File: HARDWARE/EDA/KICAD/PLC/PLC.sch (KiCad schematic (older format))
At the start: 62 parts

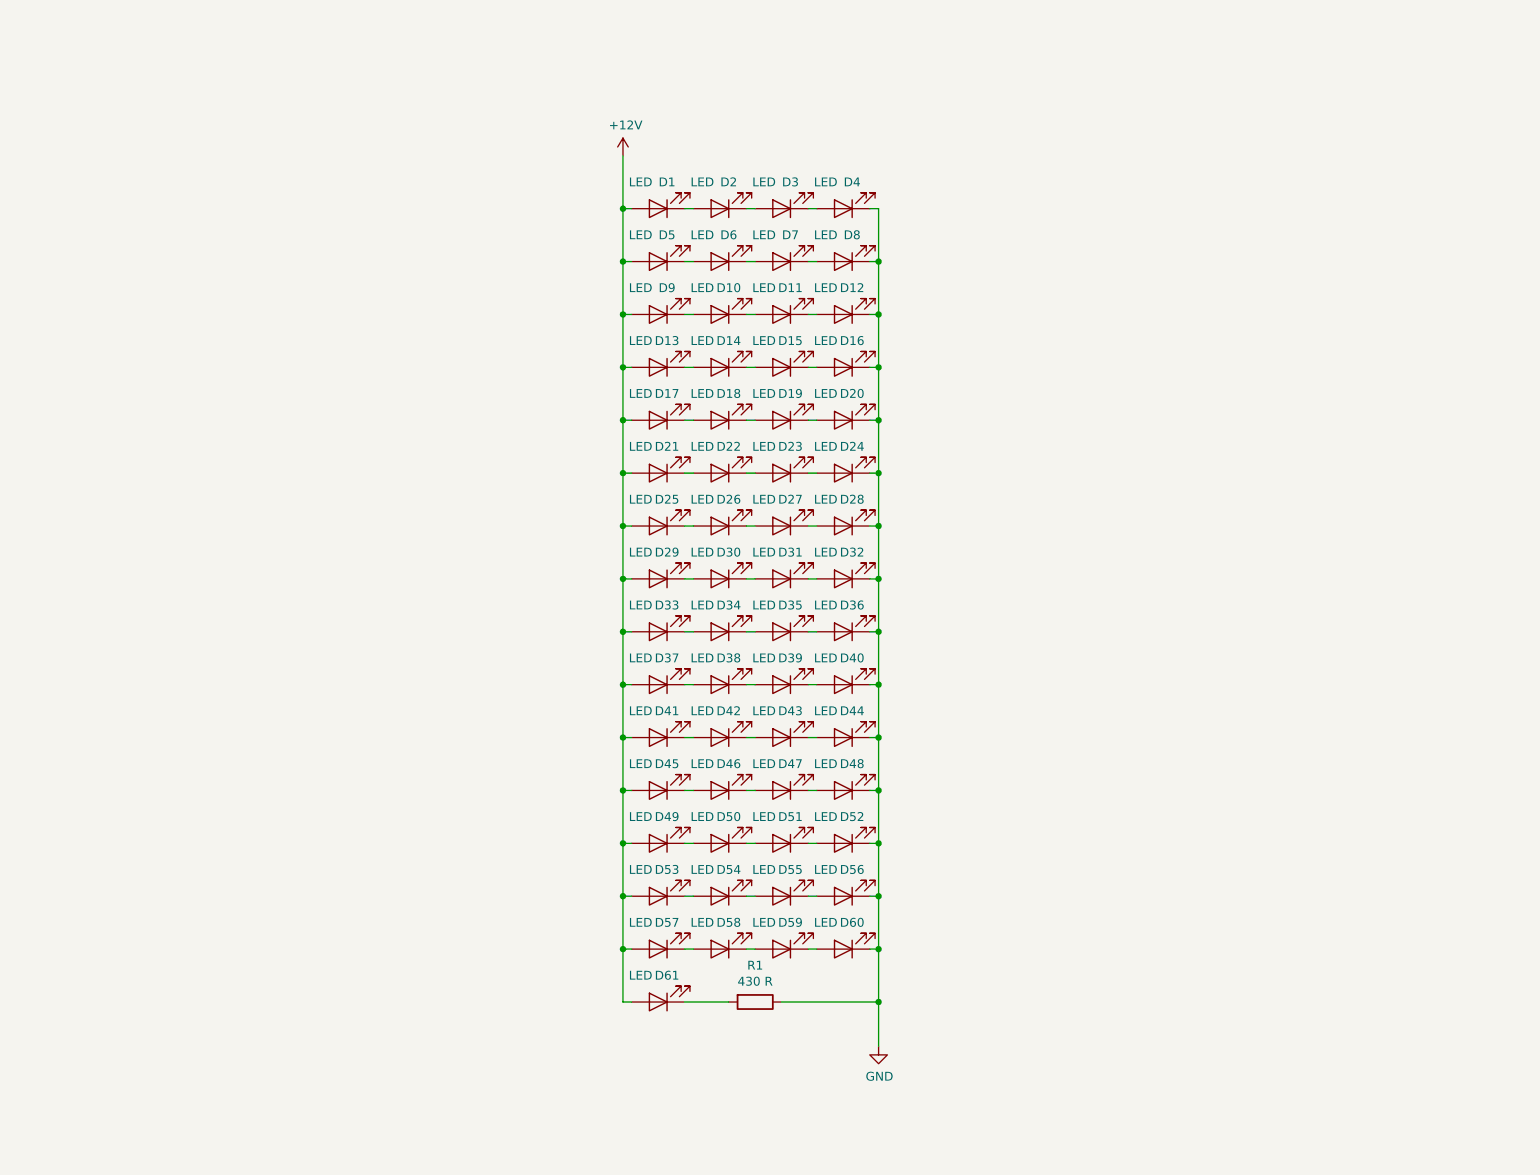
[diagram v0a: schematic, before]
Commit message: add files to toggle switch, add new componnents to plc
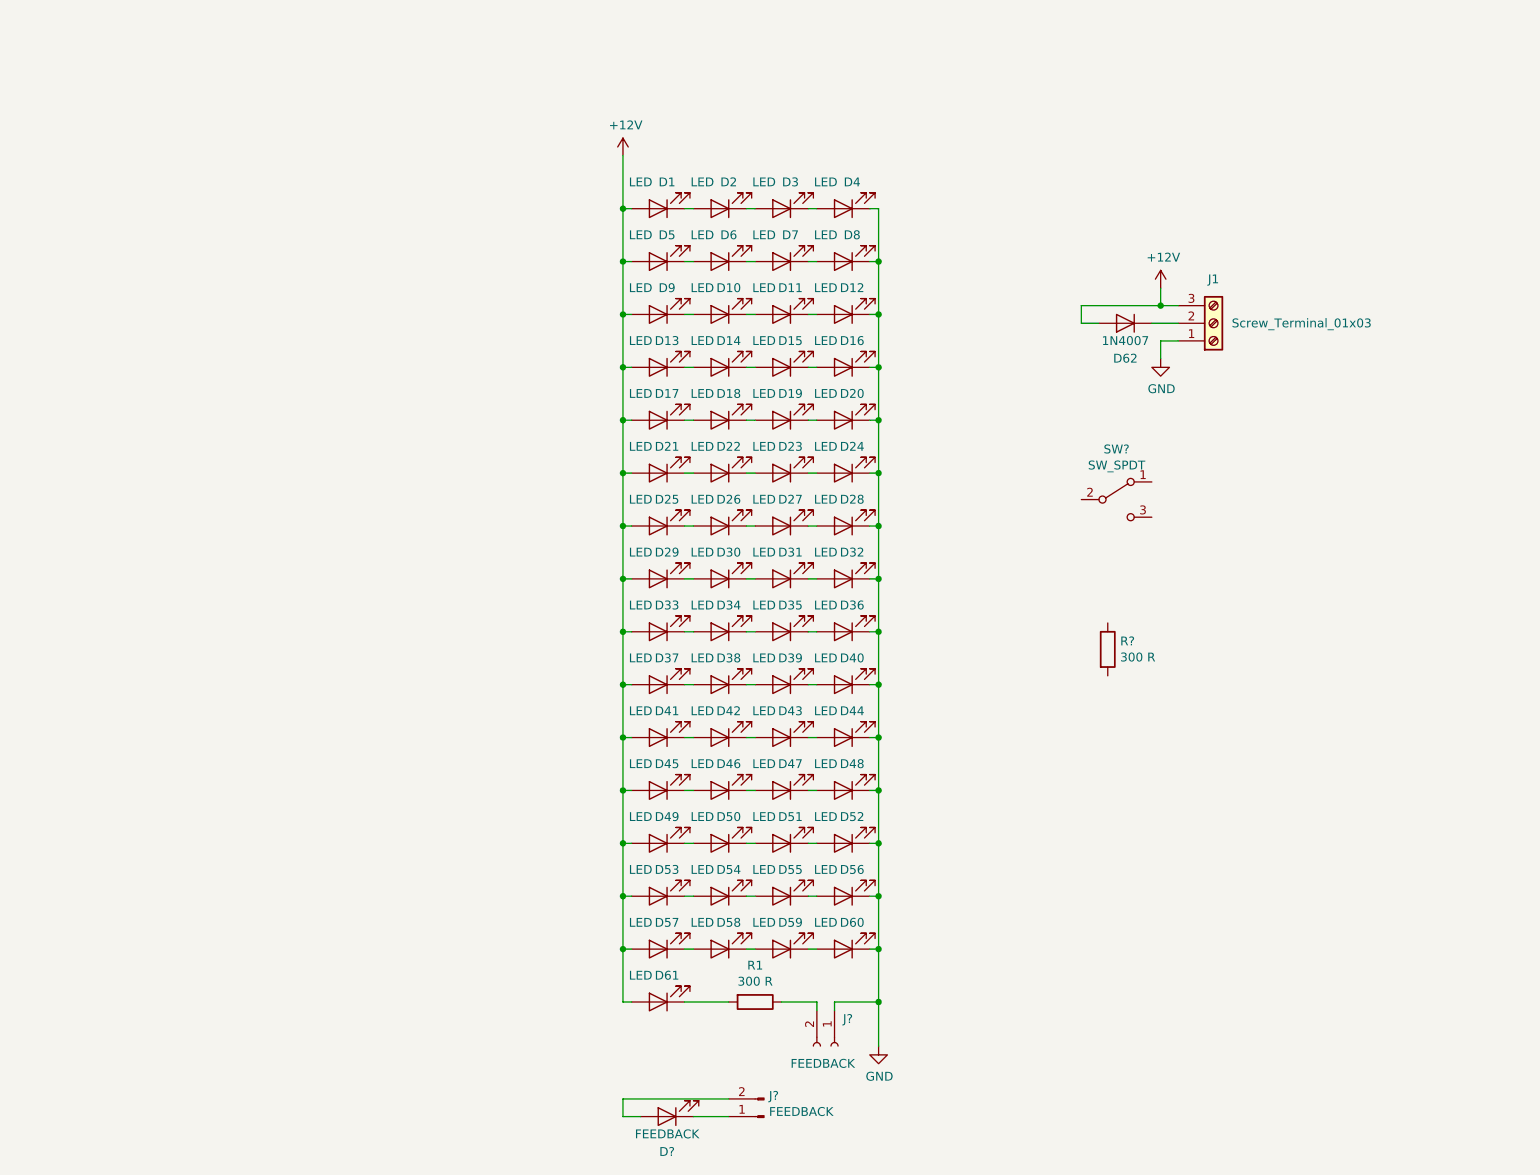
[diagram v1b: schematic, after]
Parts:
- added D62: 1N4007, Diode_THT:D_DO-41_SOD81_P10.16mm_Horizontal, symbol Diode:1N4007
- added D?: FEEDBACK, LED_THT:LED_D5.0mm_IRGrey, symbol Device:LED
- added J1: Screw_Terminal_01x03, Connector_Phoenix_MSTB:PhoenixContact_MSTBVA_2,5_3-G-5,08_1x03_P5.08mm_Vertical, symbol Connector:Screw_Terminal_01x03
- added J?: FEEDBACK, Connector_PinSocket_2.54mm:PinSocket_1x02_P2.54mm_Vertical, symbol Connector:Conn_01x02_Female
- added J?: FEEDBACK, symbol Connector:Conn_01x02_Male
- added R?: 300 R, Resistor_THT:R_Axial_DIN0411_L9.9mm_D3.6mm_P15.24mm_Horizontal, symbol Device:R
- added SW?: SW_SPDT, symbol Switch:SW_SPDT
- R1: value 430 R -> 300 R
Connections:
- net +12V: now also D62.2 (A), J1.3 (Pin_3)
- net GND: now also J1.1 (Pin_1), J?.1 (Pin_1); no longer R1.1
- new net: D62.1 (K), J1.2 (Pin_2)
- new net: J?.2 (Pin_2), R1.1
- new net: D?.1 (K), J?.1 (Pin_1)
- new net: D?.2 (A), J?.2 (Pin_2)
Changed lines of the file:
@@
 P 5200 6800
 F 0 "R1" V 4993 6800 50  0000 C CNN
-F 1 "430 R" V 5084 6800 50  0000 C CNN
+F 1 "300 R" V 5084 6800 50  0000 C CNN
 F 2 "Resistor_THT:R_Axial_DIN0207_L6.3mm_D2.5mm_P7.62mm_Horizontal" V 5130 6800 50  0001 C CNN
 F 3 "~" H 5200 6800 50  0001 C CNN
@@
 	4800 6800 5050 6800
 Wire Wire Line
-	5350 6800 5900 6800
+	5350 6800 5550 6800
 Wire Wire Line
 	4450 6800 4450 6500
@@
 	1    0    0    -1
 $EndComp
+$Comp
+L Connector:Screw_Terminal_01x03 J1
+U 1 1 61ADDB70
+P 7800 2950
+F 0 "J1" H 7800 2700 50  0000 C CNN
+F 1 "Screw_Terminal_01x03" H 8300 2950 50  0000 C CNN
+F 2 "Connector_Phoenix_MSTB:PhoenixContact_MSTBVA_2,5_3-G-5,08_1x03_P5.08mm_Vertical" H 7800 2950 50  0001 C CNN
+F 3 "~" H 7800 2950 50  0001 C CNN
+	1    7800 2950
+	1    0    0    1
+$EndComp
+$Comp
+L power:+12V #PWR03
+U 1 1 61AE4D2C
+P 7500 2750
+F 0 "#PWR03" H 7500 2600 50  0001 C CNN
+F 1 "+12V" H 7515 2923 50  0000 C CNN
+F 2 "" H 7500 2750 50  0001 C CNN
+F 3 "" H 7500 2750 50  0001 C CNN
+	1    7500 2750
+	1    0    0    -1
+$EndComp
+Wire Wire Line
+	7500 2750 7500 2850
+Wire Wire Line
+	7500 2850 7600 2850
+Wire Wire Line
+	7500 3050 7600 3050
+Connection ~ 7500 2850
+Wire Wire Line
+	7500 3150 7500 3050
+Wire Wire Line
+	7500 2850 7050 2850
+$Comp
+L power:GND #PWR04
+U 1 1 61AEFD3B
+P 7500 3150
+F 0 "#PWR04" H 7500 2900 50  0001 C CNN
+F 1 "GND" H 7505 2977 50  0000 C CNN
+F 2 "" H 7500 3150 50  0001 C CNN
+F 3 "" H 7500 3150 50  0001 C CNN
+	1    7500 3150
+	1    0    0    -1
+$EndComp
+$Comp
+L Device:LED D?
+U 1 1 61B68F6E
+P 4700 7450
+F 0 "D?" H 4700 7650 50  0000 C CNN
+F 1 "FEEDBACK" H 4700 7550 50  0000 C CNN
+F 2 "LED_THT:LED_D5.0mm_IRGrey" H 4700 7450 50  0001 C CNN
+F 3 "~" H 4700 7450 50  0001 C CNN
+	1    4700 7450
+	-1   0    0    1
+$EndComp
+$Comp
+L Diode:1N4007 D62
+U 1 1 61B4B3DB
+P 7300 2950
+F 0 "D62" H 7300 3150 50  0000 C CNN
+F 1 "1N4007" H 7300 3050 50  0000 C CNN
+F 2 "Diode_THT:D_DO-41_SOD81_P10.16mm_Horizontal" H 7300 2775 50  0001 C CNN
+F 3 "http://www.vishay.com/docs/88503/1n4001.pdf" H 7300 2950 50  0001 C CNN
+	1    7300 2950
+	-1   0    0    1
+$EndComp
+Wire Wire Line
+	7050 2950 7150 2950
+Wire Wire Line
+	7050 2850 7050 2950
+Wire Wire Line
+	7450 2950 7600 2950
+$Comp
+L Connector:Conn_01x02_Female J?
+U 1 1 61C04E26
+P 5650 7050
+F 0 "J?" V 5496 7098 50  0000 L CNN
+F 1 "FEEDBACK" V 5750 6800 50  0000 L CNN
+F 2 "Connector_PinSocket_2.54mm:PinSocket_1x02_P2.54mm_Vertical" H 5650 7050 50  0001 C CNN
+F 3 "~" H 5650 7050 50  0001 C CNN
+	1    5650 7050
+	0    1    1    0
+$EndComp
+Wire Wire Line
+	5550 6850 5550 6800
+Wire Wire Line
+	5650 6850 5650 6800
+Wire Wire Line
+	5650 6800 5900 6800
+$Comp
+L Connector:Conn_01x02_Male J?
+U 1 1 61C25C2C
+P 5250 7450
+F 0 "J?" H 5222 7332 50  0000 R CNN
+F 1 "FEEDBACK" H 5222 7423 50  0000 R CNN
+F 2 "" H 5250 7450 50  0001 C CNN
+F 3 "~" H 5250 7450 50  0001 C CNN
+	1    5250 7450
+	-1   0    0    1
+$EndComp
+Wire Wire Line
+	5050 7350 4450 7350
+Wire Wire Line
+	4450 7350 4450 7450
+Wire Wire Line
+	4450 7450 4550 7450
+Wire Wire Line
+	4850 7450 5050 7450
+$Comp
+L Device:R R?
+U 1 1 61C56BAC
+P 7200 4800
+F 0 "R?" H 7270 4846 50  0000 L CNN
+F 1 "300 R" H 7270 4755 50  0000 L CNN
+F 2 "Resistor_THT:R_Axial_DIN0411_L9.9mm_D3.6mm_P15.24mm_Horizontal" V 7130 4800 50  0001 C CNN
+F 3 "~" H 7200 4800 50  0001 C CNN
+	1    7200 4800
+	1    0    0    -1
+$EndComp
+$Comp
+L Switch:SW_SPDT SW?
+U 1 1 61C602DF
+P 7250 3950
+F 0 "SW?" H 7250 4235 50  0000 C CNN
+F 1 "SW_SPDT" H 7250 4144 50  0000 C CNN
+F 2 "" H 7250 3950 50  0001 C CNN
+F 3 "~" H 7250 3950 50  0001 C CNN
+	1    7250 3950
+	1    0    0    -1
+$EndComp

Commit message: finished new schametic
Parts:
- removed SW?: SW_SPDT, symbol Switch:SW_SPDT
- added F?: Fuse 1A, symbol Device:Fuse
- added RV? (x3): 14V, Varistor:RV_Disc_D7mm_W3.4mm_P5mm, symbol Device:Varistor
- added S?: 220/12 V, PLC_library:SW_100SP1T1B4M2QE, symbol PLC_Library:toggle_switch
- J?: footprint (none) -> Connector_PinHeader_2.54mm:PinHeader_1x02_P2.54mm_Vertical
- R?: value 300 R -> 300R 1W
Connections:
- net GND: now also RV?.1, RV?.2
- net at R?.1: now also D62.2 (A), F?.2, S?.1
- net at R?.2: now also S?.3
- net +12V renamed PWR
- net PWR: now also RV?.1, RV?.1, S?.2; no longer D62.2 (A), J1.3 (Pin_3)
- new net: F?.1, J1.3 (Pin_3)
- new net Earth: RV?.2, RV?.2
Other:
- moved on the sheet: R?
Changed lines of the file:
@@
 Connection ~ 4450 2300
 Wire Wire Line
-	4450 2300 4450 2000
+	4450 2300 4450 2050
 Connection ~ 4450 2600
 Wire Wire Line
@@
 Wire Wire Line
 	4450 6500 4450 6200
-$Comp
-L power:+12V #PWR01
-U 1 1 61B8799B
-P 4450 2000
-F 0 "#PWR01" H 4450 1850 50  0001 C CNN
-F 1 "+12V" H 4465 2173 50  0000 C CNN
-F 2 "" H 4450 2000 50  0001 C CNN
-F 3 "" H 4450 2000 50  0001 C CNN
-	1    4450 2000
-	1    0    0    -1
-$EndComp
 Wire Wire Line
 	5900 2300 5900 2600
@@
 	1    0    0    1
 $EndComp
-$Comp
-L power:+12V #PWR03
-U 1 1 61AE4D2C
-P 7500 2750
-F 0 "#PWR03" H 7500 2600 50  0001 C CNN
-F 1 "+12V" H 7515 2923 50  0000 C CNN
-F 2 "" H 7500 2750 50  0001 C CNN
-F 3 "" H 7500 2750 50  0001 C CNN
-	1    7500 2750
-	1    0    0    -1
-$EndComp
-Wire Wire Line
-	7500 2750 7500 2850
-Wire Wire Line
-	7500 2850 7600 2850
 Wire Wire Line
 	7500 3050 7600 3050
-Connection ~ 7500 2850
 Wire Wire Line
 	7500 3150 7500 3050
-Wire Wire Line
-	7500 2850 7050 2850
 $Comp
 L power:GND #PWR04
@@
 	7050 2950 7150 2950
 Wire Wire Line
-	7050 2850 7050 2950
-Wire Wire Line
 	7450 2950 7600 2950
 $Comp
@@
 F 0 "J?" H 5222 7332 50  0000 R CNN
 F 1 "FEEDBACK" H 5222 7423 50  0000 R CNN
-F 2 "" H 5250 7450 50  0001 C CNN
+F 2 "Connector_PinHeader_2.54mm:PinHeader_1x02_P2.54mm_Vertical" H 5250 7450 50  0001 C CNN
 F 3 "~" H 5250 7450 50  0001 C CNN
 	1    5250 7450
@@
 L Device:R R?
 U 1 1 61C56BAC
-P 7200 4800
-F 0 "R?" H 7270 4846 50  0000 L CNN
-F 1 "300 R" H 7270 4755 50  0000 L CNN
-F 2 "Resistor_THT:R_Axial_DIN0411_L9.9mm_D3.6mm_P15.24mm_Horizontal" V 7130 4800 50  0001 C CNN
-F 3 "~" H 7200 4800 50  0001 C CNN
-	1    7200 4800
-	1    0    0    -1
-$EndComp
-$Comp
-L Switch:SW_SPDT SW?
-U 1 1 61C602DF
-P 7250 3950
-F 0 "SW?" H 7250 4235 50  0000 C CNN
-F 1 "SW_SPDT" H 7250 4144 50  0000 C CNN
-F 2 "" H 7250 3950 50  0001 C CNN
-F 3 "~" H 7250 3950 50  0001 C CNN
-	1    7250 3950
-	1    0    0    -1
-$EndComp
+P 7050 3650
+F 0 "R?" H 7120 3696 50  0000 L CNN
+F 1 " 300R 1W" H 7120 3605 50  0000 L CNN
+F 2 "Resistor_THT:R_Axial_DIN0411_L9.9mm_D3.6mm_P15.24mm_Horizontal" V 6980 3650 50  0001 C CNN
+F 3 "~" H 7050 3650 50  0001 C CNN
+	1    7050 3650
+	-1   0    0    -1
+$EndComp
+$Comp
+L PLC_Library:toggle_switch S?
+U 1 1 61B13057
+P 7600 3950
+F 0 "S?" H 7600 4231 50  0000 C CNN
+F 1 "220/12 V" H 7600 4140 50  0000 C CNN
+F 2 "PLC_library:SW_100SP1T1B4M2QE" H 7600 3950 50  0001 L BNN
+F 3 "" H 7600 3950 50  0001 L BNN
+F 4 "Manufacturer Recommendations" H 7600 3950 50  0001 L BNN "STANDARD"
+F 5 "E" H 7600 3950 50  0001 L BNN "PARTREV"
+F 6 "29.68 mm" H 7600 3950 50  0001 L BNN "MAXIMUM_PACKAGE_HEIGHT"
+F 7 "E-Switch" H 7600 3950 50  0001 L BNN "MANUFACTURER"
+	1    7600 3950
+	-1   0    0    -1
+$EndComp
+Wire Wire Line
+	7300 4050 7050 4050
+Wire Wire Line
+	7050 4050 7050 3800
+Wire Wire Line
+	7300 3850 7200 3850
+Wire Wire Line
+	7200 3850 7200 3450
+Wire Wire Line
+	7200 3450 7050 3450
+Wire Wire Line
+	7050 3450 7050 3500
+Wire Wire Line
+	7050 3450 7050 2950
+Connection ~ 7050 3450
+Text GLabel 8850 3950 2    50   Output ~ 0
+PWR
+Text GLabel 4300 2050 0    50   Input ~ 0
+PWR
+Wire Wire Line
+	4300 2050 4450 2050
+$Comp
+L Device:Varistor RV?
+U 1 1 61BA1252
+P 8200 4200
+F 0 "RV?" H 8303 4246 50  0000 L CNN
+F 1 "14V" H 8303 4155 50  0000 L CNN
+F 2 "Varistor:RV_Disc_D7mm_W3.4mm_P5mm" V 8130 4200 50  0001 C CNN
+F 3 "~" H 8200 4200 50  0001 C CNN
+	1    8200 4200
+	1    0    0    -1
+$EndComp
+Wire Wire Line
+	8200 4050 8200 3950
+$Comp
+L power:GND #PWR?
+U 1 1 61BA7048
+P 8200 4450
+F 0 "#PWR?" H 8200 4200 50  0001 C CNN
+F 1 "GND" H 8205 4277 50  0000 C CNN
+F 2 "" H 8200 4450 50  0001 C CNN
+F 3 "" H 8200 4450 50  0001 C CNN
+	1    8200 4450
+	1    0    0    -1
+$EndComp
+Wire Wire Line
+	8200 4450 8200 4350
+Connection ~ 8200 3950
+Wire Wire Line
+	8200 3950 8550 3950
+Wire Wire Line
+	7900 3950 8200 3950
+$Comp
+L Device:Varistor RV?
+U 1 1 61BCF7CB
+P 8550 4200
+F 0 "RV?" H 8653 4246 50  0000 L CNN
+F 1 "14V" H 8653 4155 50  0000 L CNN
+F 2 "Varistor:RV_Disc_D7mm_W3.4mm_P5mm" V 8480 4200 50  0001 C CNN
+F 3 "~" H 8550 4200 50  0001 C CNN
+	1    8550 4200
+	1    0    0    -1
+$EndComp
+Wire Wire Line
+	8550 4450 8550 4350
+Wire Wire Line
+	8550 4050 8550 3950
+Connection ~ 8550 3950
+Wire Wire Line
+	8550 3950 8850 3950
+$Comp
+L power:Earth #PWR?
+U 1 1 61BDBF60
+P 8550 4450
+F 0 "#PWR?" H 8550 4200 50  0001 C CNN
+F 1 "Earth" H 8550 4300 50  0001 C CNN
+F 2 "" H 8550 4450 50  0001 C CNN
+F 3 "~" H 8550 4450 50  0001 C CNN
+	1    8550 4450
+	1    0    0    -1
+$EndComp
+$Comp
+L Device:Varistor RV?
+U 1 1 61C05D28
+P 9300 4250
+F 0 "RV?" H 9403 4296 50  0000 L CNN
+F 1 "14V" H 9403 4205 50  0000 L CNN
+F 2 "Varistor:RV_Disc_D7mm_W3.4mm_P5mm" V 9230 4250 50  0001 C CNN
+F 3 "~" H 9300 4250 50  0001 C CNN
+	1    9300 4250
+	1    0    0    -1
+$EndComp
+$Comp
+L power:Earth #PWR?
+U 1 1 61C0629D
+P 9300 4450
+F 0 "#PWR?" H 9300 4200 50  0001 C CNN
+F 1 "Earth" H 9300 4300 50  0001 C CNN
+F 2 "" H 9300 4450 50  0001 C CNN
+F 3 "~" H 9300 4450 50  0001 C CNN
+	1    9300 4450
+	1    0    0    -1
+$EndComp
+Wire Wire Line
+	9300 4400 9300 4450
+$Comp
+L power:GND #PWR?
+U 1 1 61C0B925
+P 9150 4450
+F 0 "#PWR?" H 9150 4200 50  0001 C CNN
+F 1 "GND" H 9155 4277 50  0000 C CNN
+F 2 "" H 9150 4450 50  0001 C CNN
+F 3 "" H 9150 4450 50  0001 C CNN
+	1    9150 4450
+	1    0    0    -1
+$EndComp
+Wire Wire Line
+	9150 4450 9150 4000
+Wire Wire Line
+	9150 4000 9300 4000
+Wire Wire Line
+	9300 4000 9300 4100
+$Comp
+L Device:Fuse F?
+U 1 1 61C2F40B
+P 7300 2850
+F 0 "F?" V 7103 2850 50  0000 C CNN
+F 1 "Fuse 1A" V 7194 2850 50  0000 C CNN
+F 2 "" V 7230 2850 50  0001 C CNN
+F 3 "~" H 7300 2850 50  0001 C CNN
+	1    7300 2850
+	0    1    1    0
+$EndComp
+Wire Wire Line
+	7450 2850 7600 2850
+Wire Wire Line
+	7150 2850 7050 2850
+Wire Wire Line
+	7050 2850 7050 2950
+Connection ~ 7050 2950
 $EndSCHEMATC

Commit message: remix project
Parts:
- removed R?: 300R 1W, Resistor_THT:R_Axial_DIN0411_L9.9mm_D3.6mm_P15.24mm_Horizontal, symbol Device:R
- removed S?: 220/12 V, PLC_library:SW_100SP1T1B4M2QE, symbol PLC_Library:toggle_switch
- added C1: 16V 330uf, Capacitor_THT:CP_Radial_D8.0mm_P3.50mm, symbol Device:CP
- added D64: 1N47xxA, Diode_THT:D_DO-41_SOD81_P10.16mm_Horizontal, symbol Diode:1N47xxA
- added R2: R 2W, Resistor_THT:R_Axial_DIN0411_L9.9mm_D3.6mm_P15.24mm_Horizontal, symbol Device:R
- F1: renamed from F?; footprint (none) -> Fuse:Fuseholder_Blade_Mini_Keystone_3568
- J1: value Screw_Terminal_01x03 -> pw_input
- gave numbers to parts that had none: 6
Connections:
- net GND: now also C1.2, D64.2 (A)
- net PWR: now also R2.1; no longer RV1.1, RV2.1
- net at D62.2 (A), F1.2: now also RV1.1, RV2.1, C1.1, D64.1 (K), R2.2
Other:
- note added: "0 Ohms para leds verdes"
- note added: "12 Ohms para leds Amarelos"
- note added: "12 Ohms para leds vermelhos"
- moved on the sheet: D1, D10, D11, D12, D13, D14, D15, D16, D17, D18, D19, D2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
